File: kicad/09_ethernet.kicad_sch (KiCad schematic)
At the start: 52 parts, among them J9 HR911130A, U901 KSZ9031RNXCA, U902 74LVC1G06GW, Y901 25MHz

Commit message: Placement with KiCadRoutingTools; Ethernet PHY changed to RTL8211FDI-CG
- Sheet 09 redone for the RTL8211FDI-CG (C692886; the KSZ9031 had 16 orderable, and the
  Agilex 5 card makes the same change). It runs from 3V3 only, with an internal 1.0 V core LDO
  and RGMII pads at 1.8 V from its pad LDO; all nine straps are fitted. PHYRSTB is a 3.3 V
  input, so it is driven through a 74LVC1G07 open drain. The jack LED is driven straight
  from LED2.
- The 1V2 buck (U321) is removed. Power budget and docs updated.
- make_board sets pad pin functions/types, so the placer reads the Y701 oscillator correctly.
- Placement: placement/ holds the inputs (groups, prep, intent fixes, judging chain). Seed 1
  of 12 was chosen by the quick-route judge and applied with tools/apply_placement.py.
  build_pcb.sh no longer rebuilds by default; --rebuild restores the poses.
- tools/jlc: the jlc-tools submodule.

Co-Authored-By: Claude Opus 5.5 <noreply@anthropic.com>
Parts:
- removed C923: 22u, Capacitor_SMD:C_0805_2012Metric, symbol ti135_card:C
- removed C924, C942, C943: 100n, Capacitor_SMD:C_0402_1005Metric, symbol ti135_card:C
- removed FB902: BLM15PX121SN1D, Inductor_SMD:L_0402_1005Metric, symbol ti135_card:FerriteBead_Small
- added R932, R933: 10k, Resistor_SMD:R_0402_1005Metric, symbol ti135_card:R
- C920: value 22u -> 10u
- C930: value 10u -> 1u; footprint Capacitor_SMD:C_0805_2012Metric -> Capacitor_SMD:C_0402_1005Metric
- C935: value 100n -> 1u
- C940: value 4u7 -> 1u
- R928, R929: value 1k -> 4k7
- R930: value 10k -> 4k7
- R931: value 12.1k 1% -> 2.49k 1%
- U901: value KSZ9031RNXCA -> RTL8211FDI-CG; footprint Package_DFN_QFN:QFN-48-1EP_7x7mm_P0.5mm_EP5.15x5.15mm -> Package_DFN_QFN:QFN-40-1EP_5x5mm_P0.4mm_EP3.6x3.6mm_ThermalVias; symbol ti135_card:KSZ9031RNXCA -> ti135_card:RTL8211FD; LCSC C58758 -> C692886
- U902: value 74LVC1G06GW -> 74LVC1G07GW; symbol ti135_card:74LVC1G06 -> ti135_card:74LVC1G07; LCSC (none) -> C282345
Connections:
- net phy_led_mode is gone; now on net GND: R924.2, U901.41 (GND)
- net 1V8: now also R929.1, R930.1; no longer C940.1, C941.1, R920.1, R921.1, R922.1, R923.1, R924.1, R925.1, R926.1, R927.1, U901.16 (DVDDH), U901.34 (DVDDH), U901.40 (DVDDH)
- net 3V3: now also C940.1, C941.1, R928.1, U901.29 (DVDD33), R932.1
- net GND: now also R921.2, R922.2, R923.2, R926.2, R927.2, R933.2; no longer R928.2, R929.2, R930.2, U901.29 (VSS), U901.49 (PAD_GND)
- net eth_int_n: now also R930.2, U901.31 (INTB/PMEB); no longer R927.2, U901.38 (INT_N/PME_N2)
- net eth_led_k: now also R928.2, U901.34 (LED2/CFG_LDO1); no longer U902.4
- net eth_mdc: now also U901.13 (MDC); no longer R926.2, U901.36 (MDC)
- net eth_mdi_a_N: now also U901.2 (MDIN0); no longer U901.3 (TXRXM_A)
- net eth_mdi_a_P: now also U901.1 (MDIP0); no longer U901.2 (TXRXP_A)
- net eth_mdi_b_N: now also U901.5 (MDIN1); no longer U901.6 (TXRXM_B)
- net eth_mdi_b_P: now also U901.4 (MDIP1); no longer U901.5 (TXRXP_B)
- net eth_mdi_c_N: now also U901.7 (MDIN2); no longer U901.8 (TXRXM_C)
- net eth_mdi_c_P: now also U901.6 (MDIP2); no longer U901.7 (TXRXP_C)
- net eth_mdi_d_N: now also U901.10 (MDIN3); no longer U901.11 (TXRXM_D)
- net eth_mdi_d_P: now also U901.9 (MDIP3); no longer U901.10 (TXRXP_D)
- net eth_mdio: now also R929.2, U901.14 (MDIO); no longer R925.2, U901.37 (MDIO)
- net eth_rst_n: now also U902.2, R933.1; no longer C901.1, R930.1, U901.42 (RESET_N)
- net phy_led1: now also R927.1, U901.33 (LED1/CFG_LDO0); no longer R929.1, U901.17 (LED1/PHAD0/PME_N1), U902.2
- net phy_rx_ctl: now also R922.1, U901.26 (RXCTL/PHYAD2); no longer U901.33 (RX_DV/CLK125_EN)
- net phy_rxc: now also R921.1, U901.27 (RXC/PHYAD1); no longer U901.35 (RX_CLK/PHYAD2)
- net phy_rxd0: now also R925.2, U901.25 (RXD0/RXDLY); no longer U901.32 (RXD0/MODE0)
- net phy_rxd1: now also R924.1, U901.24 (RXD1/TXDLY); no longer U901.31 (RXD1/MODE1)
- net phy_rxd2: now also R923.1, U901.23 (RXD2/PLLOFF); no longer U901.28 (RXD2/MODE2)
- net phy_rxd3: now also R920.2, U901.22 (RXD3/PHYAD0); no longer U901.27 (RXD3/MODE3)
- net phy_tx_ctl: now also U901.19 (TXCTL); no longer U901.25 (TX_EN)
- net phy_txc: now also U901.20 (TXC); no longer U901.24 (GTX_CLK)
- net phy_txd0: now also U901.18 (TXD0); no longer U901.19 (TXD0)
- net phy_txd1: now also U901.17 (TXD1); no longer U901.20 (TXD1)
- net phy_txd2: now also U901.16 (TXD2); no longer U901.21 (TXD2)
- net phy_txd3: now also U901.15 (TXD3); no longer U901.22 (TXD3)
- net phy_xi: now also U901.36 (XTAL_IN); no longer U901.46 (XI)
- net phy_xo: now also U901.37 (XTAL_OUT); no longer U901.45 (XO)
- net rgmii_rxd0: no longer R920.2
- net rgmii_rxd1: no longer R921.2
- net rgmii_rxd2: no longer R922.2
- net rgmii_rxd3: no longer R923.2
- removed net 1V2: C930.1, C931.1, C932.1, C933.1, C934.1, C935.1, C936.1, U901.14 (DVDDL), U901.18 (DVDDL), U901.23 (DVDDL), U901.26 (DVDDL), U901.30 (DVDDL), U901.39 (DVDDL), U901.4 (AVDDL), U901.9 (AVDDL)
- net phy_avddh renamed phy_avdd33
- net phy_avdd33: now also U901.11 (AVDD33), U901.40 (AVDD33); no longer U901.1 (AVDDH), U901.12 (AVDDH)
- removed net phy_avddl_pll: U901.44 (AVDDL_PLL)
- net phy_iset renamed phy_rset
- net phy_rset: now also U901.39 (RSET); no longer U901.48 (ISET)
- removed net phy_led2: R928.1, U901.15 (LED2/PHYAD1)
- new net phy_dvdd_rg: C935.1, C936.1, R920.1, R925.1, U901.28 (DVDD_RG)
- new net phy_led0: R926.1, U901.32 (LED0/CFG_EXT)
- new net phy_rstb: C901.1, R932.2, U901.12 (PHYRSTB), U902.4
- new net phy_vdd10: C930.1, C931.1, C932.1, C933.1, C934.1, U901.21 (DVDD10), U901.3 (AVDD10), U901.30 (LDO_OUT), U901.38 (AVDD10), U901.8 (AVDD10)
- no-connect marks 5 -> 4
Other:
- note added: "25 MHz crystal 3225, 27 p load (Agilex card values), +/-50 ppm total; place at the PHY"
- note added: "AVDD33 (pins 11, 40) through a ferrite: 10u + 2 x 100n"
- note added: "DVDD33 (pin 29)"
- note added: "DVDD_RG: RGMII pad LDO output (1.8 V), caps only"
- note added: "Jack LED: green anode via R950 to 3V3, cathode on PHY LED2 (3.3 V pin, active low with its CFG_LDO1 pull-up R928). Program LCR for link/activity."
- note added: "LDO_OUT 1.0 V -> AVDD10 (3, 8, 38) + DVDD10 (21) only: 1u + 4 x 100n (>= 0.1u, Table 9.2)"
- note added: "PHYRSTB is a 3.3 V input: U902 74LVC1G07 (1V8 supply) open drain, R932 10k to 3V3, C901 filter. R933 holds eth_rst_n low until the FPGA drives it (PHY in reset during configuration)."
- note added: "RTL8211FDI-CG gigabit PHY, RGMII at 1.8 V (internal pad LDO) to bank 4B, PHY address 1. 3.3 V only: core 1.0 V from its own LDO. J9 = HanRun HR911130A magjack (green LED from LED2, yellow spare), placed per MECHANICAL.md."
- note added: "Straps 4k7: PHYAD = 001 (RXD3 up, RXC/RXCTL down), PLLOFF/TXDLY = 0, RXDLY = 1 (RX pins to DVDD_RG); CFG_EXT = 0 (LED0 down), CFG_LDO = 10 (LED1 down, LED2 up to 3V3) -> 1.8 V RGMII pads. MDIO/INT_N pull-ups."
- note removed: "1V2 DVDDL/AVDDL (8 pins): 10u + 6 x 100n"
- note removed: "1V8 DVDDH (3 pins): 4u7 + 3 x 100n"
- note removed: "25 MHz crystal 3225, 27 p load (Agilex card values); place at the PHY"
- note removed: "AVDDH (3V3) and AVDDL_PLL (1V2) through ferrites (Agilex FB1/FB2)"
- note removed: "Jack LED: LED1 (1.8 V, active high with its PHYAD0 pull-down) -> U902 open-drain inverter -> LED cathode; anode via R950 to 3V3. Verify LED1 polarity at bring-up."
- note removed: "KSZ9031RNX gigabit PHY, RGMII at 1.8 V to bank 4B. Values and straps from the Agilex 5 card (address 0, RGMII mode, single-LED mode). J9 = HanRun HR911130A magjack (green LED used, yellow spare), placed per MECHANICAL.md."
- note removed: "Straps / pulls (1V8): MODE0..3 = 1 (RGMII), LED_MODE = 1 (single LED), PHYAD = 0, MDIO/MDC/INT pull-ups, RESET_N pull-down (PHY held in reset until the FPGA drives it)."
- moved on the sheet: C901, C935, C936, C940, C941, C951

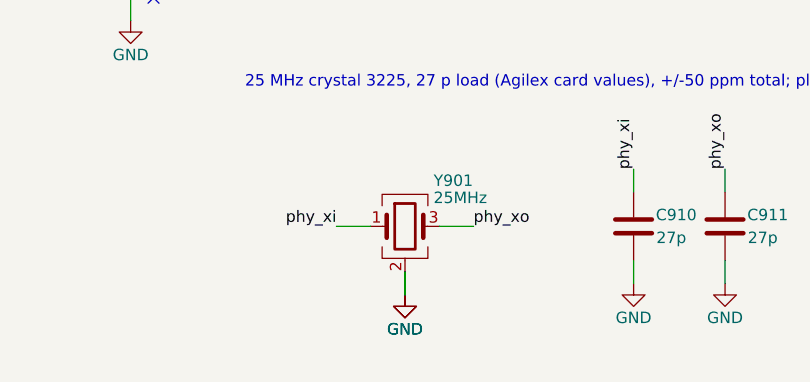
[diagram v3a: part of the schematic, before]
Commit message: LPDDR4 hand routing: Agilex DRAM escape copied, byte lanes routed, DQ swizzle by hand
- U801 decoupling = the Agilex U12 set (sheet 08: 29 x 100n 0201, 22u/1u 0402, LCSC from the
  Agilex card), placed at the Agilex positions on the same via pairs; R802 (ZQ) at R43's spot;
  CA/CKE T-branches on B.Cu copied (tools/ddr/copy_dram_escape.py)
- LPDDR4 vias not on a BGA ball removed (T-branch centre vias kept)
- Schematic: #PWR/#FLG references made unique per sheet (prefix = sheet number); the
  duplicates blocked Update PCB from Schematic
- DQ swizzle now edited by hand in the schematic (bytes 0 and 2); efinity/pinplan/lpddr4_swizzle.json
  is not updated yet
- Byte lanes routed by hand (work in progress)

Known open (WIP): byte 2 - ddr_dq22 on two U501 balls (AA16, W16), ddr_dq21 has no U501 ball;
DRC shows 2 shorts at U501 Y16/W16 (dq21/dq17 tracks).

Co-Authored-By: Claude Opus 5.5 <noreply@anthropic.com>
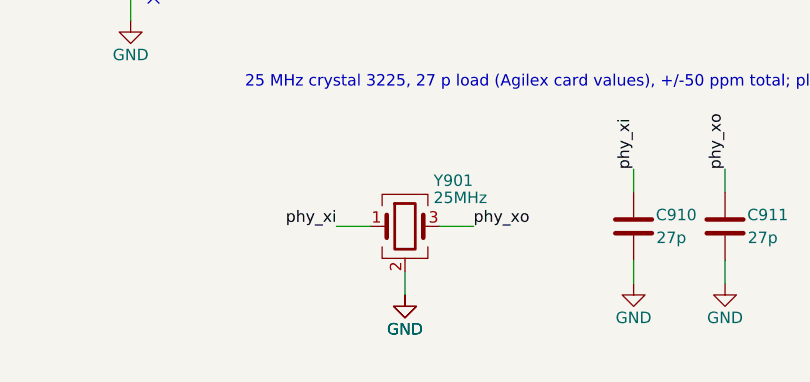
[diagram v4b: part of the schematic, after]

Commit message: LCSC numbers for all JLC parts; Y701 -> YXC OT322525MJBA4SL
- tools/set_lcsc.py: one table (value, footprint) -> LCSC, fills empty LCSC fields in the
  sheets; 312 symbols. JLC basic parts where available, cap voltages checked per rail,
  VCORE divider 0.1 % (no 0.5 % in stock). Board fields synced with add_parts.py.
- Y701: the SiT8924 has no JLC stock; now YXC OT322525MJBA4SL (C669088, 3225), EN tied
  to 1V8. R701/C701 moved 0.5 mm to clear its courtyard. Netlist change: Y701 pin 1 -> 1V8.
- Only U501 (Ti135) is left without LCSC (global sourcing / consigned).
- DRC: schematic parity 0.

Co-Authored-By: Claude Opus 5.5 <noreply@anthropic.com>
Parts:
- C901, C921, C922, C931, C932, C933, C934, C936, C941, C950, C951: LCSC (none) -> C1525
- C910, C911: LCSC (none) -> C1557
- C920: LCSC (none) -> C15850
- C930, C935, C940: LCSC (none) -> C52923
- FB901: LCSC (none) -> C88970
- R901, R902, R903, R904, R905, R906, R907, R908, R909, R910, R911, R912: LCSC (none) -> C25092
- R920, R921, R922, R923, R924, R925, R926, R927, R928, R929, R930: LCSC (none) -> C25900
- R931: LCSC (none) -> C25884
- R932, R933: LCSC (none) -> C25744
- R950: LCSC (none) -> C25104
- Y901: LCSC (none) -> C70593
